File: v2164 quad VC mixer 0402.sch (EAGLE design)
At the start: 32 parts, among them IC1 TL072JD

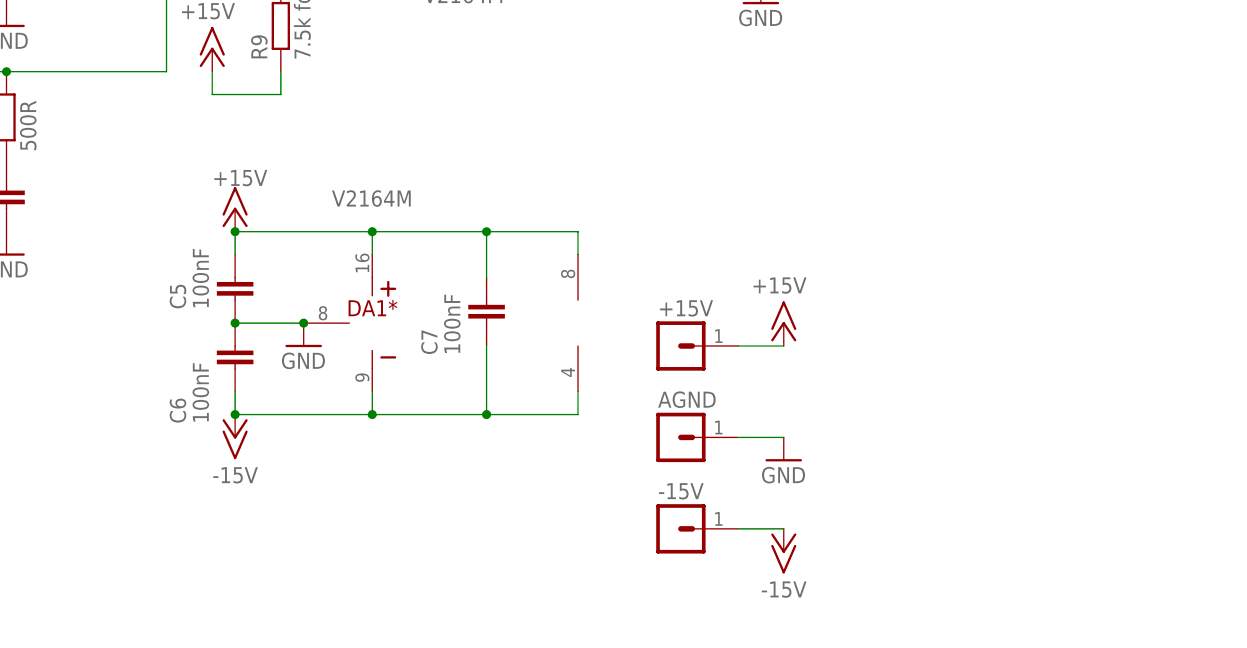
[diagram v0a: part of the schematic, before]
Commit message: Added optional shottky diodes
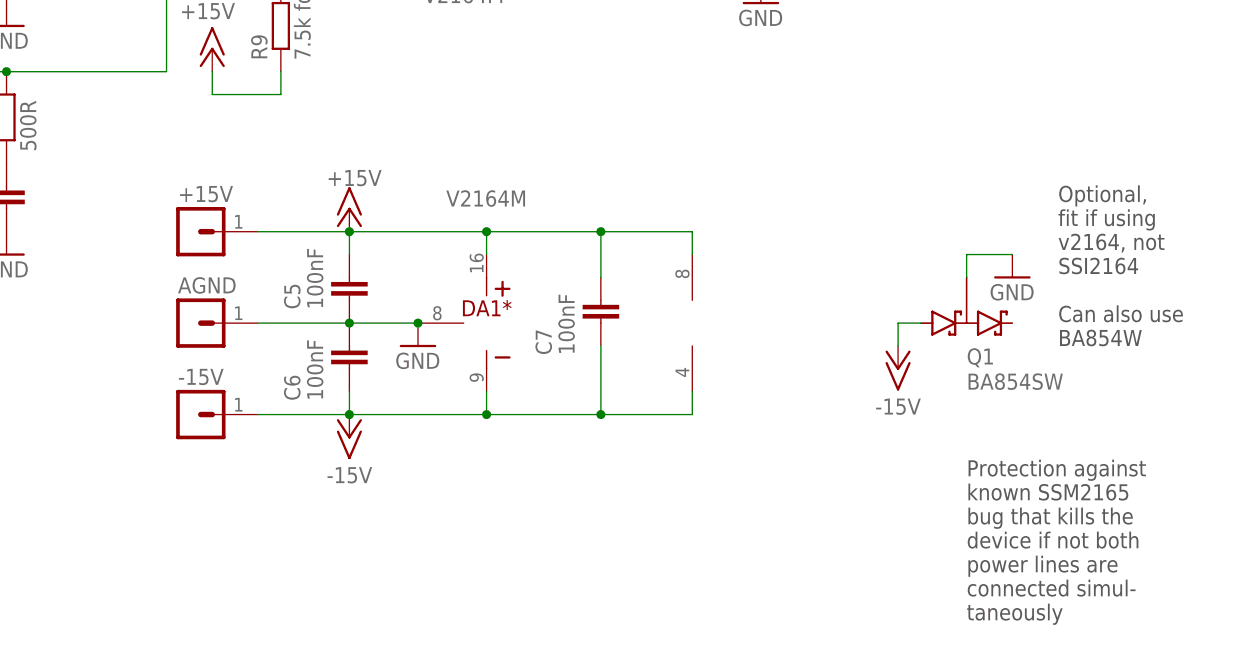
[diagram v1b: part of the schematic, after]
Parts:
- added Q1: BA854SW, joakim:BA854SW
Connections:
- net -15V: now also Q1.A1
- net GND: now also Q1.K1A2
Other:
- note added: "Optional, fit if using v2164, not SSI2164 Can also use BA854W"
- note added: "Protection against known SSM2165 bug that kills the device if not both power lines are connected simul- taneously"
- moved on the sheet: +15V, -15V, AGND, C5, C6, C7, DA1*
